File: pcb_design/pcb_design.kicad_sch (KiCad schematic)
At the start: 0 parts

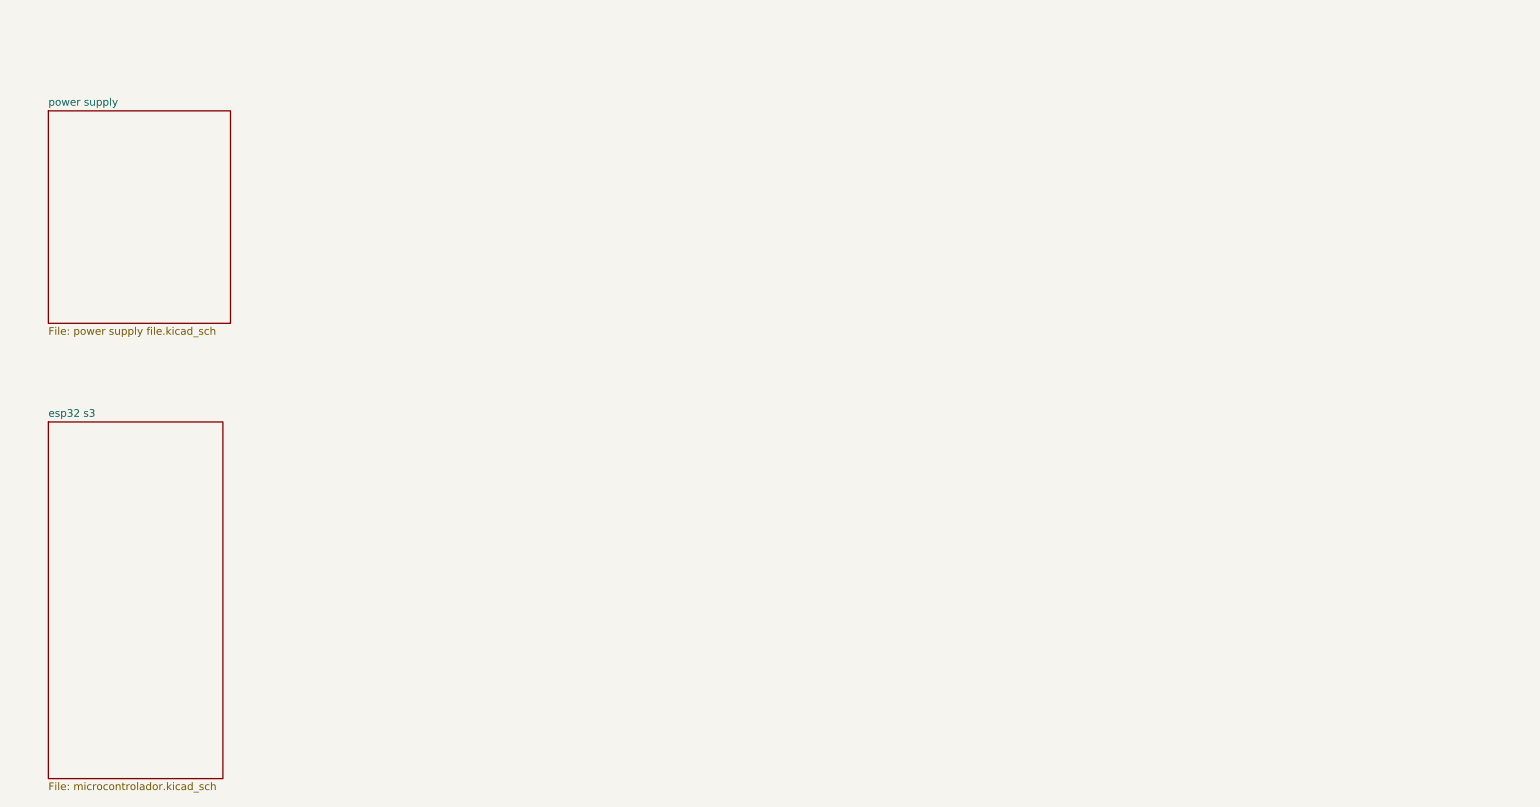
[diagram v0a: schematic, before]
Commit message: cambio de regulador de alto iq por reguladores de bajo iq separados uno para sensores y otro para micro y comunicacion usando el lt8610, apagado de alimentacion de sensores atravez de mosfet canal p
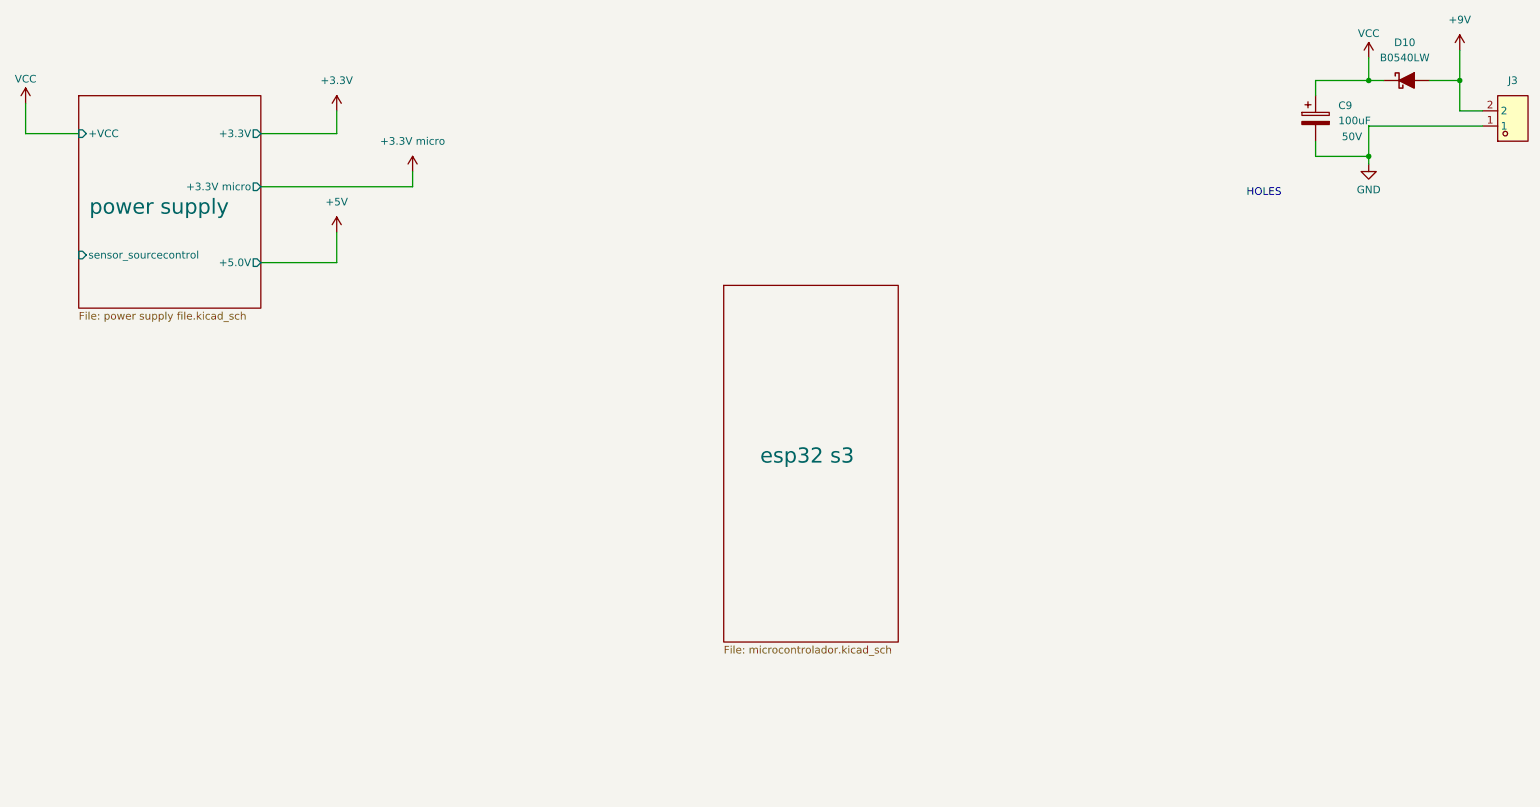
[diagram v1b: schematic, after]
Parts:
- added C9: 100uF, Capacitor_SMD_AKL:CP_Elec_6.3x7.7, symbol Capacitor_AKL:CP_SMD_D6.3mm_H7.7mm
- added D10: B0540LW, Diode_SMD_AKL:D_SOD-123, symbol PCM_Diode_Schottky_AKL:B0540LW
- added J3: DB128L-5.08-2P-BK-S, EasyEDA:CONN-TH_2P-P5.08_DB128L-5.08-2P-BK-S, symbol EasyEDA:DB128L-5.08-2P-BK-S
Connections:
- new net +9V: D10.2 (A), J3.2
- new net GND: C9.2, J3.1
- new net VCC: C9.1, D10.1 (K)
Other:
- sheet power supply ports: added +3.3V, +3.3V micro, +5.0V, +VCC, sensor_sourcecontrol; removed none
- note added: "HOLES"
